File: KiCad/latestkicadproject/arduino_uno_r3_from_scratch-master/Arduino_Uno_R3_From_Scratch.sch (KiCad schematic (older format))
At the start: 0 parts

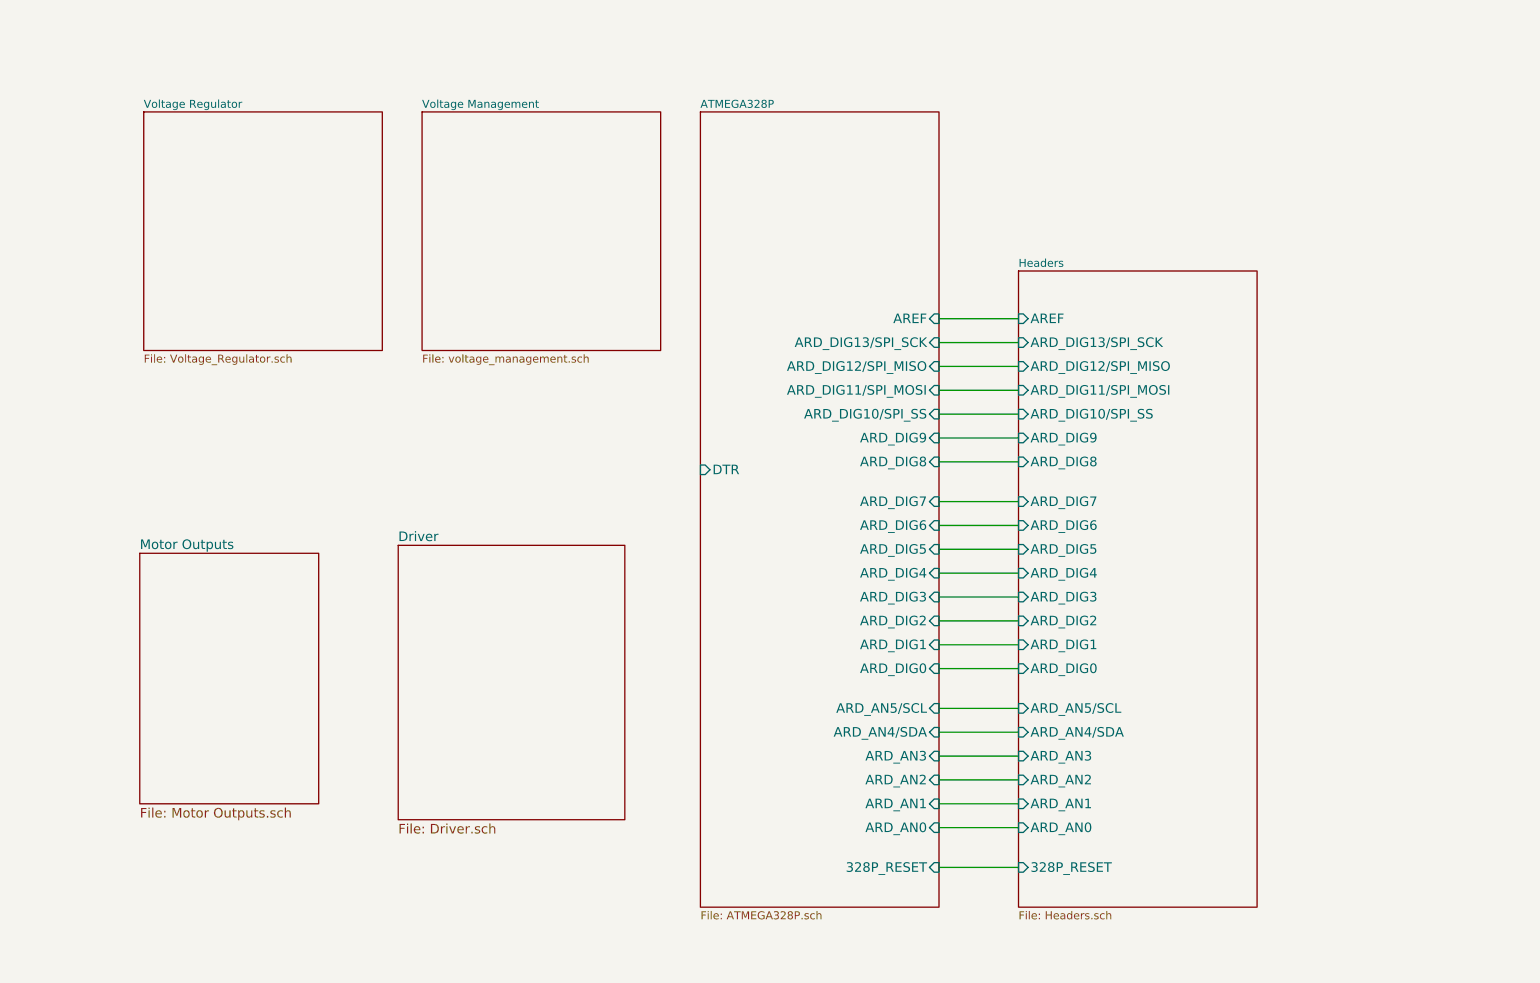
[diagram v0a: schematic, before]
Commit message: 28feb
Aanpassing KiCad+deel footprints
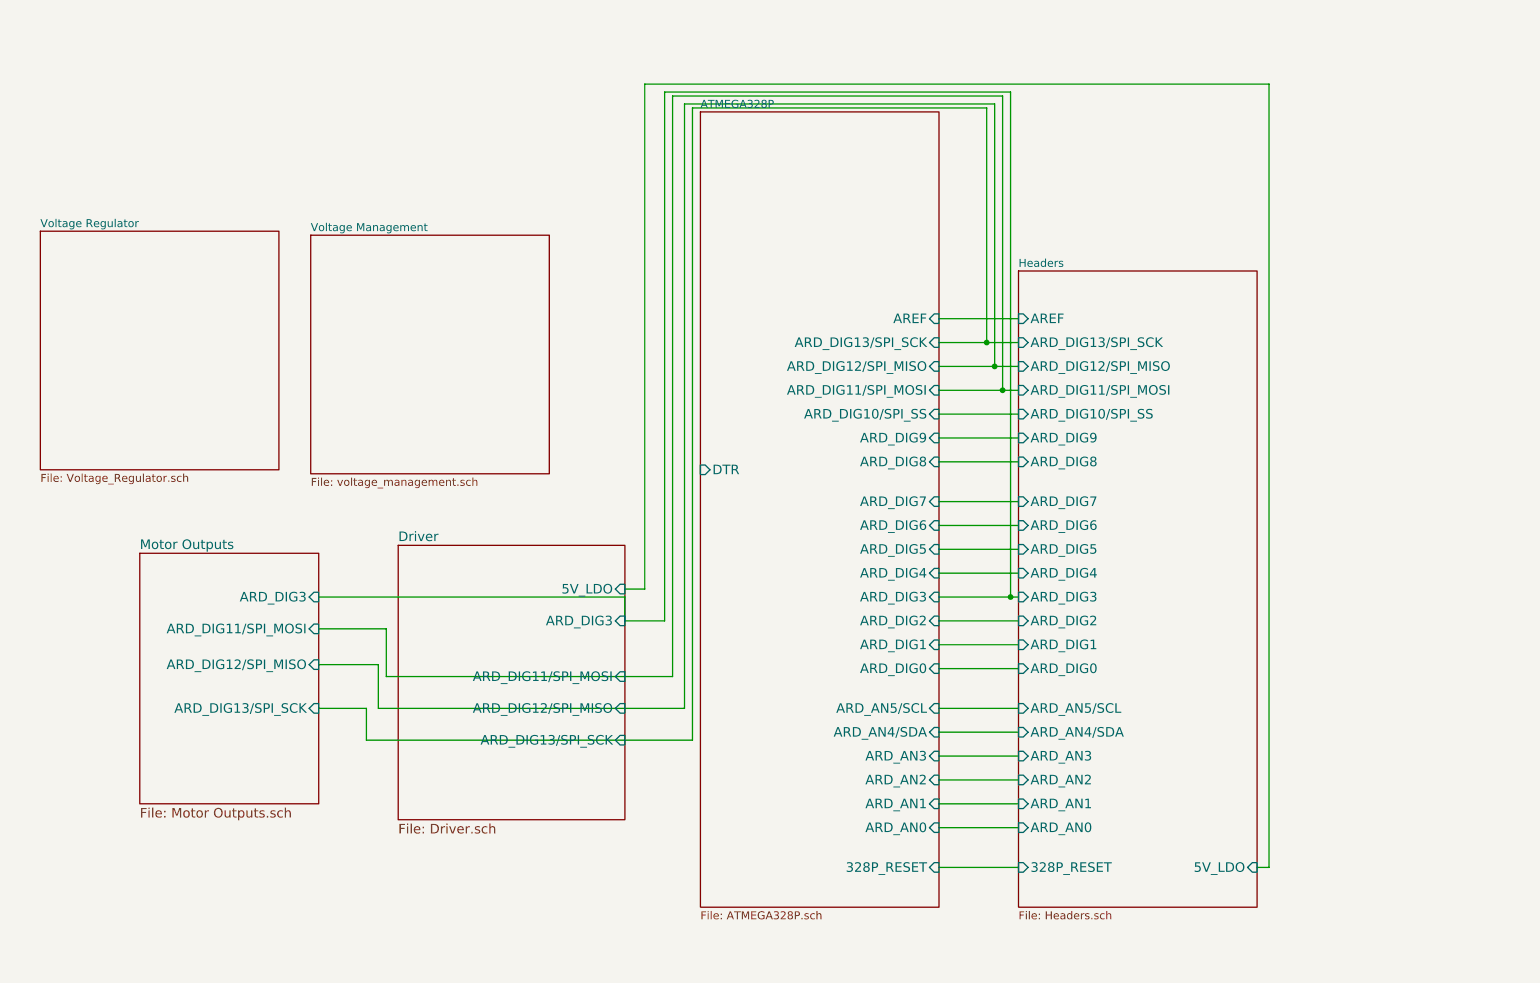
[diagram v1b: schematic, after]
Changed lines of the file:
@@
 $EndDescr
 $Sheet
-S 2050 1400 1500 1500
+S 1400 2150 1500 1500
 U 55CCFEA2
 F0 "Voltage Regulator" 50
@@
 $EndSheet
 $Sheet
-S 3800 1400 1500 1500
+S 3100 2175 1500 1500
 U 55D0D7E6
 F0 "Voltage Management" 50
@@
 F22 "ARD_DIG1" I L 7550 4750 60
 F23 "ARD_DIG0" I L 7550 4900 60
+F24 "5V_LDO" I R 9050 6150 60
+$EndSheet
+Wire Wire Line
+	7050 2700 7550 2700
+Wire Wire Line
+	7550 2850 7050 2850
+Wire Wire Line
+	7050 3000 7550 3000
+Wire Wire Line
+	7550 3150 7050 3150
+Wire Wire Line
+	7050 3300 7550 3300
+Wire Wire Line
+	7550 3450 7050 3450
+Wire Wire Line
+	7050 3600 7550 3600
+Wire Wire Line
+	7550 3850 7050 3850
+Wire Wire Line
+	7050 4000 7550 4000
+Wire Wire Line
+	7550 4150 7050 4150
+Wire Wire Line
+	7050 4300 7550 4300
+Wire Wire Line
+	7050 4600 7550 4600
+Wire Wire Line
+	7550 4750 7050 4750
+Wire Wire Line
+	7050 4900 7550 4900
+Wire Wire Line
+	7550 5150 7050 5150
+Wire Wire Line
+	7050 5300 7550 5300
+Wire Wire Line
+	7550 5450 7050 5450
+Wire Wire Line
+	7050 5600 7550 5600
+Wire Wire Line
+	7550 5750 7050 5750
+Wire Wire Line
+	7050 5900 7550 5900
+Wire Wire Line
+	7550 6150 7050 6150
+$Sheet
+S 2025 4175 1125 1575
+U 5A845897
+F0 "Motor Outputs" 60
+F1 "Motor Outputs.sch" 60
+F2 "ARD_DIG3" I R 3150 4450 60
+F3 "ARD_DIG11/SPI_MOSI" I R 3150 4650 60
+F4 "ARD_DIG12/SPI_MISO" I R 3150 4875 60
+F5 "ARD_DIG13/SPI_SCK" I R 3150 5150 60
+$EndSheet
+$Sheet
+S 3650 4125 1425 1725
+U 5A845975
+F0 "Driver" 60
+F1 "Driver.sch" 60
+F2 "5V_LDO" I R 5075 4400 60
+F3 "ARD_DIG3" I R 5075 4600 60
+F4 "ARD_DIG12/SPI_MISO" I R 5075 5150 60
+F5 "ARD_DIG13/SPI_SCK" I R 5075 5350 60
+F6 "ARD_DIG11/SPI_MOSI" I R 5075 4950 60
 $EndSheet
 $Sheet
@@
 $EndSheet
 Wire Wire Line
-	7050 2700 7550 2700
+	7050 4450 7550 4450
 Wire Wire Line
-	7550 2850 7050 2850
+	5325 1275 7500 1275
+Connection ~ 7500 4450
 Wire Wire Line
-	7050 3000 7550 3000
+	7500 1275 7500 4450
 Wire Wire Line
-	7550 3150 7050 3150
+	5375 4950 5375 1300
 Wire Wire Line
-	7050 3300 7550 3300
+	5375 1300 7450 1300
 Wire Wire Line
-	7550 3450 7050 3450
+	7450 1300 7450 3150
+Connection ~ 7450 3150
 Wire Wire Line
-	7050 3600 7550 3600
+	5450 5150 5450 1350
 Wire Wire Line
-	7550 3850 7050 3850
+	5450 1350 7400 1350
 Wire Wire Line
-	7050 4000 7550 4000
+	7400 1350 7400 3000
+Connection ~ 7400 3000
 Wire Wire Line
-	7550 4150 7050 4150
+	5500 1375 7350 1375
 Wire Wire Line
-	7050 4300 7550 4300
+	7350 1375 7350 2850
+Connection ~ 7350 2850
 Wire Wire Line
-	7550 4450 7050 4450
+	5325 4600 5075 4600
 Wire Wire Line
-	7050 4600 7550 4600
+	3575 4950 5375 4950
 Wire Wire Line
-	7550 4750 7050 4750
+	3525 5150 5450 5150
 Wire Wire Line
-	7050 4900 7550 4900
+	3450 5350 5500 5350
 Wire Wire Line
-	7550 5150 7050 5150
+	5325 1275 5325 4600
 Wire Wire Line
-	7050 5300 7550 5300
+	5500 5350 5500 1375
 Wire Wire Line
-	7550 5450 7050 5450
+	3150 4450 5075 4450
 Wire Wire Line
-	7050 5600 7550 5600
+	5075 4450 5075 4600
 Wire Wire Line
-	7550 5750 7050 5750
+	3575 4950 3575 4650
 Wire Wire Line
-	7050 5900 7550 5900
+	3575 4650 3150 4650
 Wire Wire Line
-	7550 6150 7050 6150
-$Sheet
-S 2025 4175 1125 1575
-U 5A845897
-F0 "Motor Outputs" 60
-F1 "Motor Outputs.sch" 60
-$EndSheet
-$Sheet
-S 3650 4125 1425 1725
-U 5A845975
-F0 "Driver" 60
-F1 "Driver.sch" 60
-$EndSheet
+	3150 4875 3525 4875
+Wire Wire Line
+	3525 4875 3525 5150
+Wire Wire Line
+	3450 5350 3450 5150
+Wire Wire Line
+	3450 5150 3150 5150
+Wire Wire Line
+	9050 6150 9125 6150
+Wire Wire Line
+	9125 6150 9125 1225
+Wire Wire Line
+	9125 1225 5200 1225
+Wire Wire Line
+	5200 1225 5200 4400
+Wire Wire Line
+	5200 4400 5075 4400
 $EndSCHEMATC

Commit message: Aanpassing KiCad PCB ontwerp + footprints
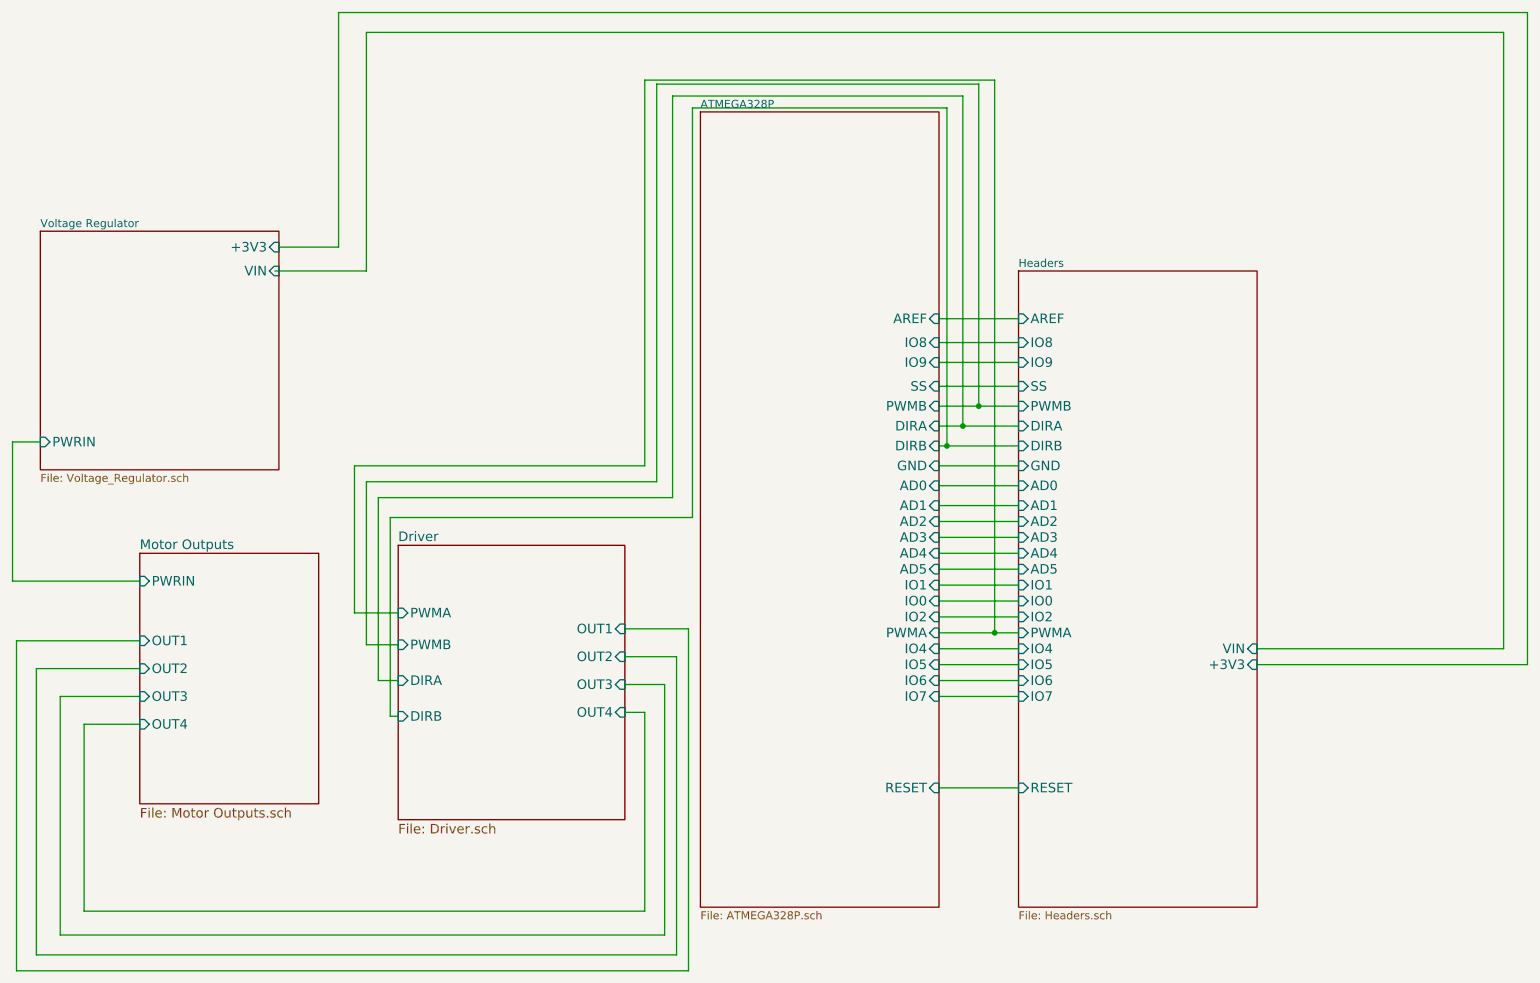
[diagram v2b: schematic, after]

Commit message: pcb routing
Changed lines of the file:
@@
 LIBS:LP2985-33DBVR
 LIBS:degson
+LIBS:PHT6NQ10T_135
 EELAYER 25 0
 EELAYER END
@@
 	7050 5650 7550 5650
 Wire Wire Line
-	2875 2400 3450 2400
-Wire Wire Line
 	3450 2400 3450 900
 Wire Wire Line
@@
 Wire Wire Line
 	3600 5200 3650 5200
+Wire Wire Line
+	3450 2400 2900 2400
 $EndSCHEMATC

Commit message: PCB routing v1
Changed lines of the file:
@@
 LIBS:degson
 LIBS:PHT6NQ10T_135
+LIBS:L298P
 EELAYER 25 0
 EELAYER END
@@
 F10 "DIRA" I L 7550 3375 60
 F11 "DIRB" I L 7550 3500 60
-F12 "GND" I L 7550 3625 60
-F13 "AD0" I L 7550 3750 60
-F14 "AD1" I L 7550 3875 60
-F15 "AD2" I L 7550 3975 60
-F16 "AD3" I L 7550 4075 60
-F17 "AD4" I L 7550 4175 60
-F18 "AD5" I L 7550 4275 60
-F19 "IO1" I L 7550 4375 60
-F20 "IO0" I L 7550 4475 60
-F21 "IO2" I L 7550 4575 60
-F22 "PWMA" I L 7550 4675 60
-F23 "IO4" I L 7550 4775 60
-F24 "IO5" I L 7550 4875 60
-F25 "IO6" I L 7550 4975 60
-F26 "IO7" I L 7550 5075 60
+F12 "AD0" I L 7550 3750 60
+F13 "AD1" I L 7550 3875 60
+F14 "AD2" I L 7550 3975 60
+F15 "AD3" I L 7550 4075 60
+F16 "AD4" I L 7550 4175 60
+F17 "AD5" I L 7550 4275 60
+F18 "IO1" I L 7550 4375 60
+F19 "IO0" I L 7550 4475 60
+F20 "IO2" I L 7550 4575 60
+F21 "PWMA" I L 7550 4675 60
+F22 "IO4" I L 7550 4775 60
+F23 "IO5" I L 7550 4875 60
+F24 "IO6" I L 7550 4975 60
+F25 "IO7" I L 7550 5075 60
+F26 "GND" I L 7550 5400 60
 $EndSheet
 $Sheet
@@
 F22 "IO6" I R 7050 4975 60
 F23 "IO7" I R 7050 5075 60
-F24 "GND" I R 7050 3625 60
+F24 "GND" I R 7050 5400 60
 $EndSheet
 Wire Wire Line
@@
 Wire Wire Line
 	7050 3750 7550 3750
-Wire Wire Line
-	7050 3625 7550 3625
 Wire Wire Line
 	7050 3500 7550 3500
@@
 Wire Wire Line
 	3450 2400 2900 2400
+Wire Wire Line
+	7050 5400 7550 5400
 $EndSCHEMATC

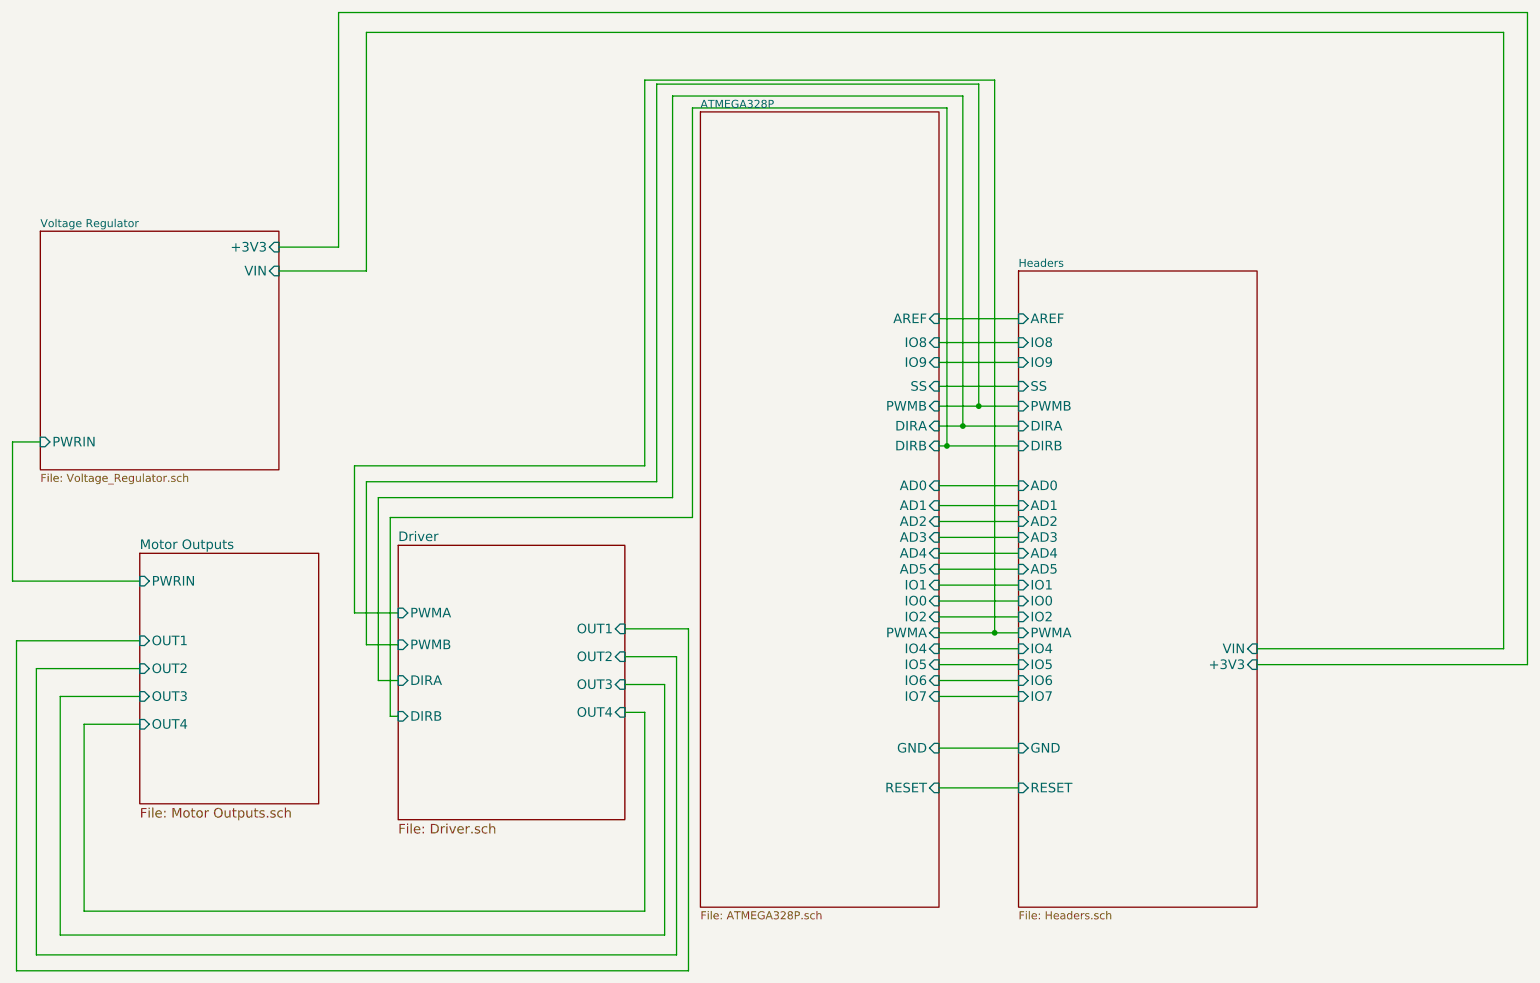
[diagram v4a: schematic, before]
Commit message: correctie gnd-fouten
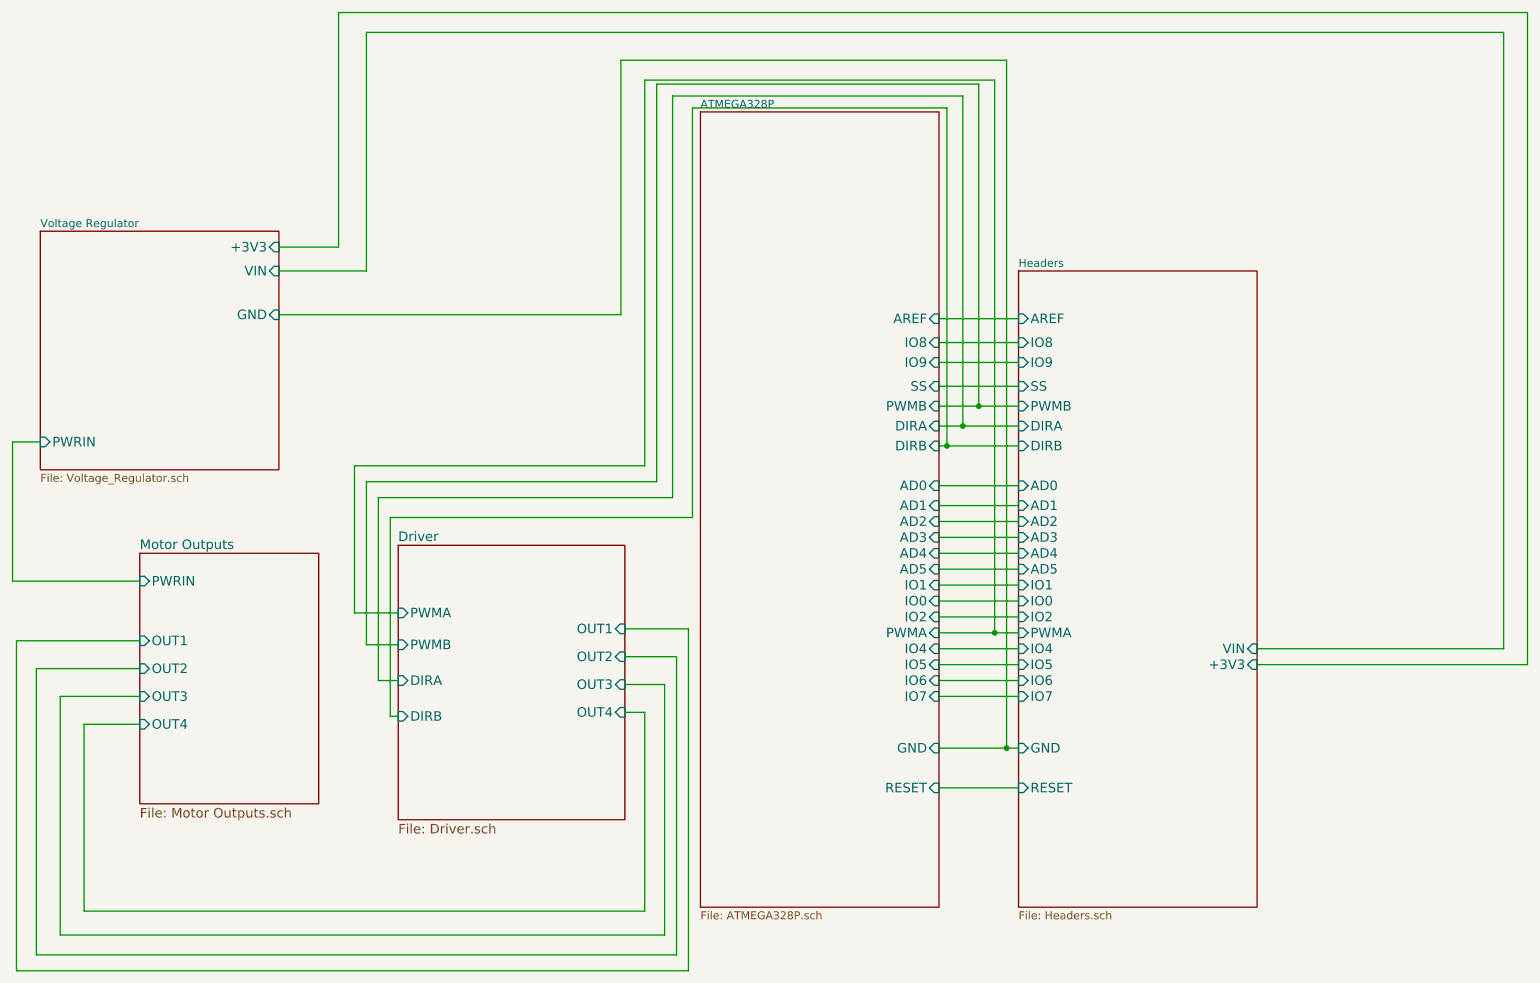
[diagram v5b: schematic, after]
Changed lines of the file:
@@
 F3 "VIN" I R 2900 2400 60
 F4 "+3V3" I R 2900 2250 60
+F5 "GND" I R 2900 2675 60
 $EndSheet
 $Sheet
@@
 Wire Wire Line
 	7050 5400 7550 5400
+Wire Wire Line
+	2900 2675 5050 2675
+Wire Wire Line
+	5050 2675 5050 1075
+Wire Wire Line
+	5050 1075 7475 1075
+Wire Wire Line
+	7475 1075 7475 5400
+Connection ~ 7475 5400
 $EndSCHEMATC

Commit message: verbeteringen kicad
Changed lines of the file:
@@
 F5 "OUT3" I L 2025 5075 60
 F6 "OUT4" I L 2025 5250 60
+F7 "GND" I R 3150 4525 60
 $EndSheet
 $Sheet
@@
 F8 "OUT4" I R 5075 5175 60
 F9 "OUT3" I R 5075 5000 60
+F10 "GND" I L 3650 4275 60
 $EndSheet
 $Sheet
@@
 	7475 1075 7475 5400
 Connection ~ 7475 5400
+Wire Wire Line
+	3650 4275 3650 2675
+Connection ~ 3650 2675
+Wire Wire Line
+	3150 4525 3300 4525
+Wire Wire Line
+	3300 4525 3300 2675
+Connection ~ 3300 2675
 $EndSCHEMATC
